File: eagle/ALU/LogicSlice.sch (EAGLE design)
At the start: 0 parts

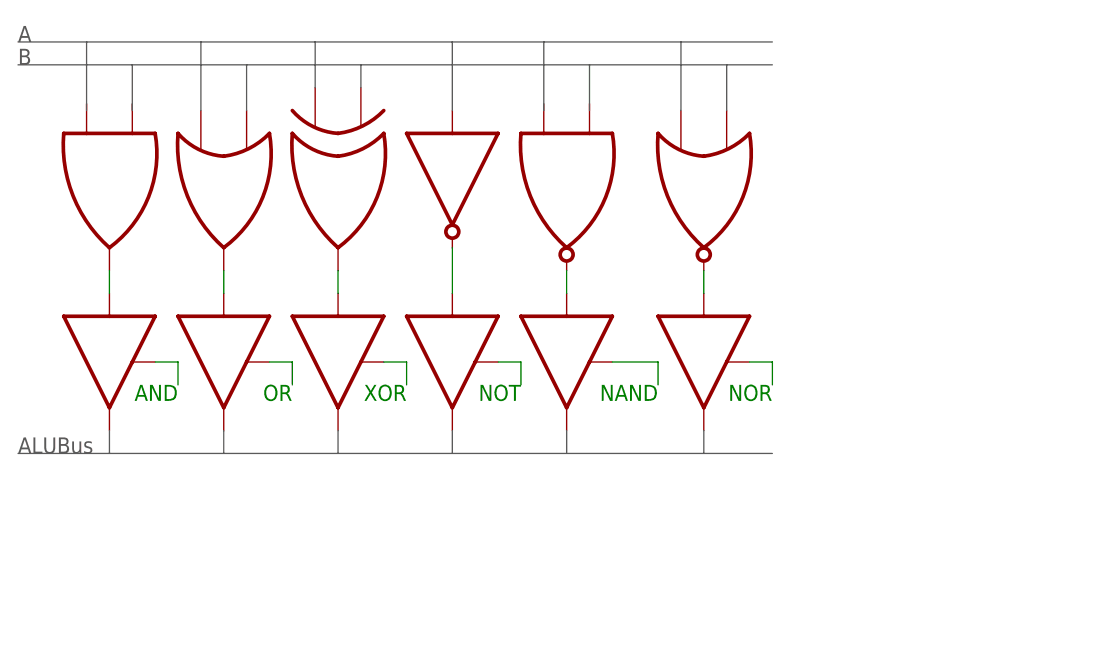
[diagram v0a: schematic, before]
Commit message: Eagle schematics now use library
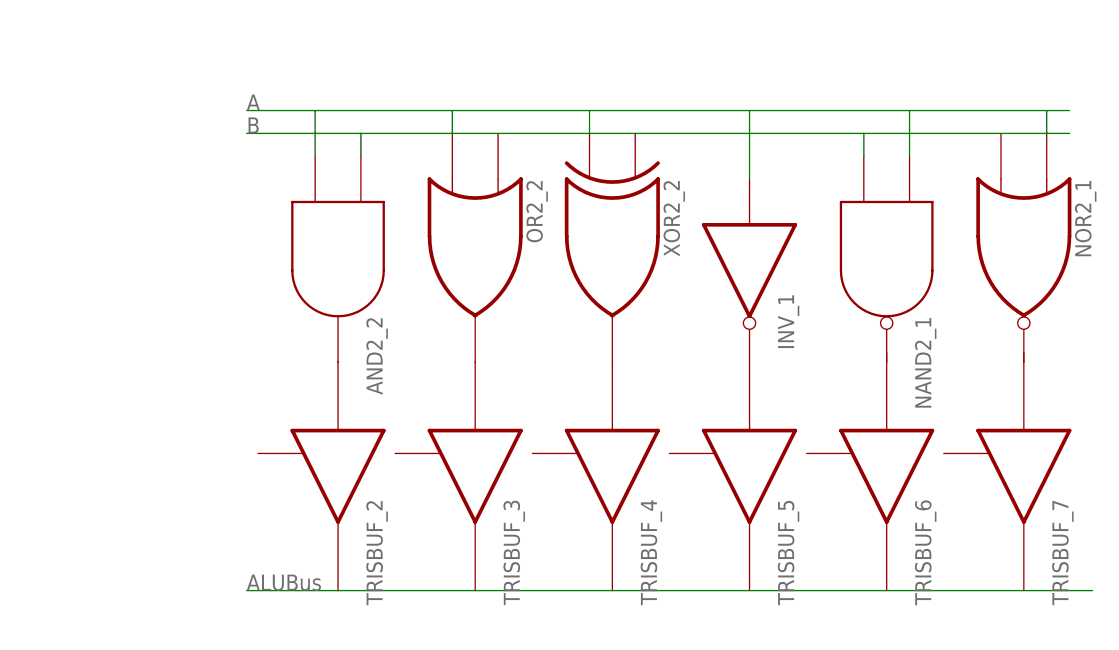
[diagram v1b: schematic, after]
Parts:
- added AND2_2: AND2, c035u:AND2
- added INV_1: INV, c035u:INV
- added NAND2_1: NAND2, c035u:NAND2
- added NOR2_1: NOR2, c035u:NOR2
- added OR2_2: OR2, c035u:OR2
- added TRISBUF_2, TRISBUF_3, TRISBUF_4, TRISBUF_5, TRISBUF_6, TRISBUF_7: TRISBUF, c035u:TRISBUF
- added XOR2_2: XOR2, c035u:XOR2
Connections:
- new net N$1: AND2_2.O, TRISBUF_2.I
- new net N$2: OR2_2.O, TRISBUF_3.I
- new net N$3: TRISBUF_4.I, XOR2_2.O
- new net N$4: INV_1.O, TRISBUF_5.I
- new net N$5: NAND2_1.O, TRISBUF_6.I
- new net N$6: NOR2_1.O, TRISBUF_7.I
- new net N$9: AND2_2.A, AND2_2.I1, INV_1.I, NAND2_1.A, NAND2_1.I1, OR2_2.I1, XOR2_2.I1
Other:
- note removed: "AND"
- note removed: "NAND"
- note removed: "NOR"
- note removed: "NOT"
- note removed: "OR"
- note removed: "XOR"

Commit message: Schematics small improvements
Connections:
- net N$9: now also NOR2_1.I0, NOR2_1.I1, OR2_2.I0, XOR2_2.I0
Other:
- note added: "AND"
- note added: "NAND"
- note added: "NOR"
- note added: "NOT"
- note added: "OR"
- note added: "XOR"
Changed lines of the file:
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@@
 <text x="17.78" y="116.84" size="1.778" layer="95">A</text>
 <text x="17.78" y="114.3" size="1.778" layer="95">B</text>
+<text x="22.86" y="78.74" size="1.778" layer="95" rot="R180">AND</text>
+<text x="38.1" y="78.74" size="1.778" layer="95" rot="R180">OR</text>
+<text x="38.1" y="78.74" size="1.778" layer="95" rot="R180">OR</text>
+<text x="53.34" y="78.74" size="1.778" layer="95" rot="R180">XOR</text>
+<text x="68.58" y="78.74" size="1.778" layer="95" rot="R180">NOT</text>
+<text x="84.836" y="78.74" size="1.778" layer="95" rot="R180">NAND</text>
+<text x="99.06" y="78.74" size="1.778" layer="95" rot="R180">NOR</text>
 </plain>
 <instances>
@@
 </instances>
 <busses>
+<bus name="B$1">
+<segment>
+<wire x1="17.78" y1="63.5" x2="109.22" y2="63.5" width="0.1524" layer="92"/>
+</segment>
+</bus>
 </busses>
 <nets>
@@
 </segment>
 </net>
-<net name="N$7" class="0">
-<segment>
-<wire x1="17.78" y1="63.5" x2="111.76" y2="63.5" width="0.1524" layer="91"/>
-</segment>
-</net>
 <net name="N$9" class="0">
 <segment>
@@
 <wire x1="40.64" y1="116.84" x2="55.88" y2="116.84" width="0.1524" layer="91"/>
 <wire x1="55.88" y1="116.84" x2="73.66" y2="116.84" width="0.1524" layer="91"/>
-<wire x1="73.66" y1="116.84" x2="91.44" y2="116.84" width="0.1524" layer="91"/>
-<wire x1="91.44" y1="116.84" x2="106.68" y2="116.84" width="0.1524" layer="91"/>
-<wire x1="106.68" y1="116.84" x2="109.22" y2="116.84" width="0.1524" layer="91"/>
-<wire x1="109.22" y1="114.3" x2="106.68" y2="114.3" width="0.1524" layer="91"/>
-<wire x1="106.68" y1="114.3" x2="86.36" y2="114.3" width="0.1524" layer="91"/>
-<wire x1="86.36" y1="114.3" x2="55.88" y2="114.3" width="0.1524" layer="91"/>
-<wire x1="55.88" y1="114.3" x2="40.64" y2="114.3" width="0.1524" layer="91"/>
+<wire x1="73.66" y1="116.84" x2="86.36" y2="116.84" width="0.1524" layer="91"/>
+<wire x1="86.36" y1="116.84" x2="101.6" y2="116.84" width="0.1524" layer="91"/>
+<wire x1="101.6" y1="116.84" x2="109.22" y2="116.84" width="0.1524" layer="91"/>
+<wire x1="101.6" y1="114.3" x2="91.44" y2="114.3" width="0.1524" layer="91"/>
+<wire x1="91.44" y1="114.3" x2="60.96" y2="114.3" width="0.1524" layer="91"/>
+<wire x1="60.96" y1="114.3" x2="55.88" y2="114.3" width="0.1524" layer="91"/>
+<wire x1="55.88" y1="114.3" x2="45.72" y2="114.3" width="0.1524" layer="91"/>
+<wire x1="45.72" y1="114.3" x2="40.64" y2="114.3" width="0.1524" layer="91"/>
 <wire x1="40.64" y1="114.3" x2="30.48" y2="114.3" width="0.1524" layer="91"/>
 <wire x1="30.48" y1="114.3" x2="17.78" y2="114.3" width="0.1524" layer="91"/>
-<wire x1="106.68" y1="116.84" x2="106.68" y2="114.3" width="0.1524" layer="91"/>
-<pinref part="NAND2_1" gate="G$1" pin="A"/>
-<wire x1="91.44" y1="116.84" x2="91.44" y2="111.76" width="0.1524" layer="91"/>
-<pinref part="NAND2_1" gate="G$1" pin="I1"/>
-<wire x1="86.36" y1="114.3" x2="86.36" y2="111.76" width="0.1524" layer="91"/>
 <pinref part="INV_1" gate="G$1" pin="I"/>
 <wire x1="73.66" y1="116.84" x2="73.66" y2="109.22" width="0.1524" layer="91"/>
@@
 <pinref part="AND2_2" gate="G$1" pin="A"/>
 <wire x1="30.48" y1="114.3" x2="30.48" y2="111.76" width="0.1524" layer="91"/>
+<junction x="25.4" y="116.84"/>
+<junction x="30.48" y="114.3"/>
+<junction x="40.64" y="116.84"/>
+<pinref part="OR2_2" gate="G$1" pin="I0"/>
+<junction x="45.72" y="114.3"/>
+<junction x="55.88" y="116.84"/>
+<pinref part="XOR2_2" gate="G$1" pin="I0"/>
+<junction x="60.96" y="114.3"/>
+<junction x="73.66" y="116.84"/>
+<pinref part="NOR2_1" gate="G$1" pin="I1"/>
+<pinref part="NAND2_1" gate="G$1" pin="I1"/>
+<wire x1="86.36" y1="111.76" x2="86.36" y2="116.84" width="0.1524" layer="91"/>
+<pinref part="NAND2_1" gate="G$1" pin="A"/>
+<wire x1="91.44" y1="111.76" x2="91.44" y2="114.3" width="0.1524" layer="91"/>
+<wire x1="109.22" y1="114.3" x2="106.68" y2="114.3" width="0.1524" layer="91"/>
+<wire x1="106.68" y1="114.3" x2="101.6" y2="114.3" width="0.1524" layer="91"/>
+<wire x1="101.6" y1="114.3" x2="101.6" y2="116.84" width="0.1524" layer="91"/>
+<junction x="86.36" y="116.84"/>
+<junction x="91.44" y="114.3"/>
+<junction x="101.6" y="116.84"/>
+<pinref part="NOR2_1" gate="G$1" pin="I0"/>
+<junction x="106.68" y="114.3"/>
 </segment>
 </net>
